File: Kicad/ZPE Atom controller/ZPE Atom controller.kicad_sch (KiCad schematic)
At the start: 48 parts, among them IC1 TC4424AVPA, J1 50 ohm 21 turns, P1 CONN_01X18, P2 CONN_01X18, Q1 2N2222, Q2 IRF3205, SW1 ON/OFF, SW2 SW_SPST, SW3 SW_SPST, SW4 SW_SPST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

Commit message: Added caps to inputs of the pots.
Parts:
- added C11, C12, C13, C14, C15: 100nF, Capacitor_THT:C_Disc_D5.0mm_W2.5mm_P5.00mm, symbol Device:C
- C10, C9: value 10nF -> 100nF
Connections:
- net GND: now also C11.2, C12.2, C13.2, C14.2, C15.2
- net IO32: now also C12.1
- net IO34: now also C14.1
- net IO35: now also C15.1
- net IO36: now also C13.1
- net IO39: now also C11.1
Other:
- moved on the sheet: DutyCycle1, Freq_fine1, Freq_rough1, Freq_super_fine1, Resolution1

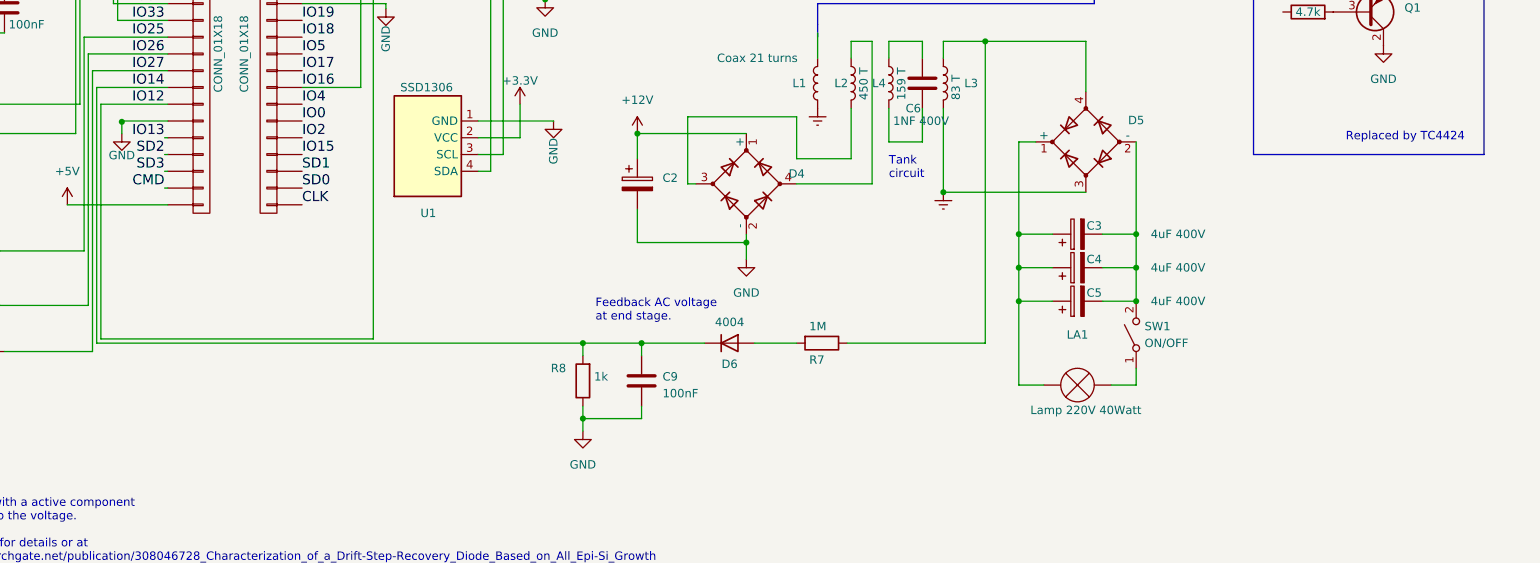
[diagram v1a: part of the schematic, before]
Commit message: Added DC to AC inverter
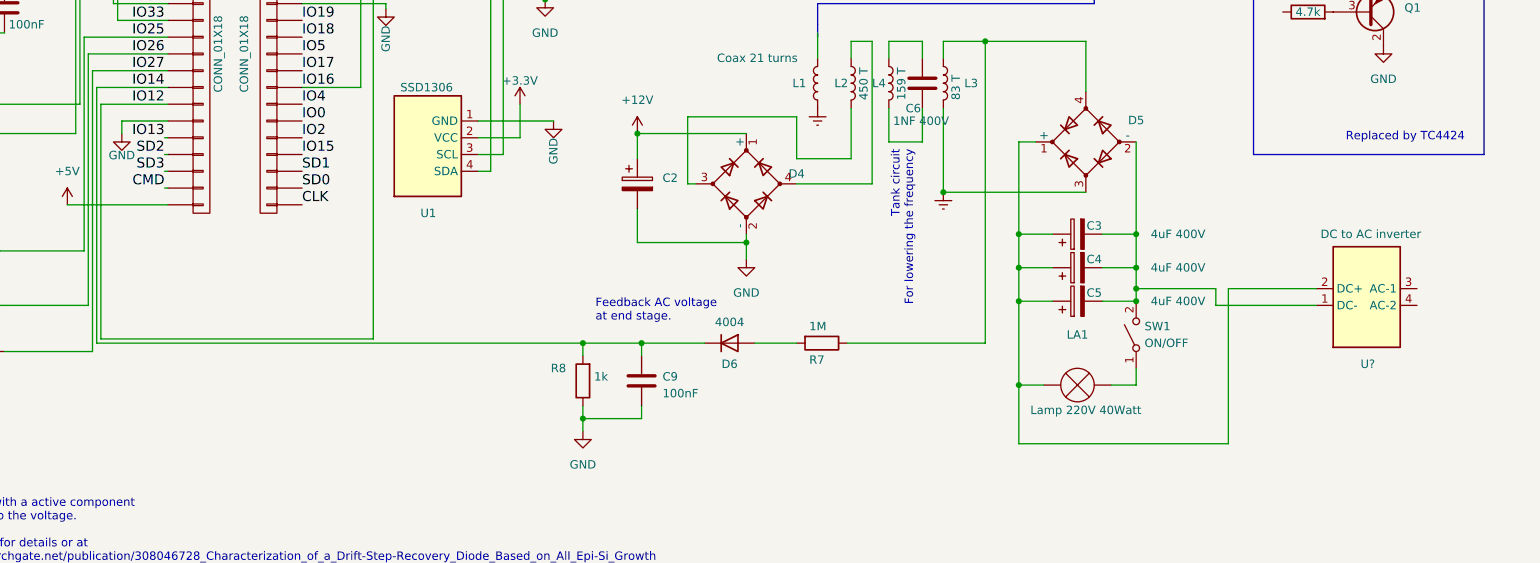
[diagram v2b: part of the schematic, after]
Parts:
- added U?: DC to AC inverter, DC to AC inverter, symbol Memory_EEPROM:24AA02-OT
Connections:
- net at C3.1, C4.1, C5.1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: now also U?.2 (DC+)
- net at C3.2, C4.2, C5.2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: now also U?.1 (DC-)
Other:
- note added: "Tank circuit For lowering the frequency"
- note removed: "Tank circuit"
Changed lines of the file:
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@@
   (junction (at 137.16 147.955) (diameter 0) (color 0 0 0 0)
   )
+  (junction (at 203.2 154.305) (diameter 0) (color 0 0 0 0)
+  )
   (junction (at 51.435 91.44) (diameter 0) (color 0 0 0 0)
   )
@@
   (junction (at 22.606 127) (diameter 0) (color 0 0 0 0)
   )
+  (junction (at 220.98 139.7) (diameter 0) (color 0 0 0 0)
+  )
   (junction (at 66.675 66.04) (diameter 0) (color 0 0 0 0)
   )
@@
   (junction (at 170.18 27.305) (diameter 0) (color 0 0 0 0)
   )
-  (junction (at 67.31 114.427) (diameter 0) (color 0 0 0 0)
-  )
   (junction (at 33.02 127) (diameter 0) (color 0 0 0 0)
   )
@@
     (stroke (width 0) (type default))
   )
+  (wire (pts (xy 248.285 139.7) (xy 234.95 139.7))
+    (stroke (width 0) (type default))
+  )
   (wire (pts (xy 123.19 86.36) (xy 123.19 121.92))
     (stroke (width 0) (type default))
@@
     (stroke (width 0) (type default))
   )
+  (wire (pts (xy 233.045 139.7) (xy 233.045 142.24))
+    (stroke (width 0) (type default))
+  )
   (wire (pts (xy 215.9 131.445) (xy 220.98 131.445))
     (stroke (width 0) (type default))
@@
     (stroke (width 0) (type default))
   )
+  (wire (pts (xy 220.98 139.7) (xy 220.98 136.525))
+    (stroke (width 0) (type default))
+  )
   (wire (pts (xy 46.355 100.965) (xy 36.195 100.965))
     (stroke (width 0) (type default))
@@
     (stroke (width 0) (type default))
   )
-  (wire (pts (xy 67.31 114.427) (xy 67.31 114.3))
-    (stroke (width 0) (type default))
-  )
   (wire (pts (xy 208.28 141.605) (xy 203.2 141.605))
     (stroke (width 0) (type default))
@@
     (stroke (width 0) (type default))
   )
+  (wire (pts (xy 233.045 139.7) (xy 220.98 139.7))
+    (stroke (width 0) (type default))
+  )
   (wire (pts (xy 49.53 93.345) (xy 51.435 93.345))
     (stroke (width 0) (type default))
@@
     (stroke (width 0) (type default))
   )
+  (wire (pts (xy 203.2 163.195) (xy 203.2 154.305))
+    (stroke (width 0) (type default))
+  )
   (wire (pts (xy 170.18 46.355) (xy 170.18 48.895))
     (stroke (width 0) (type default))
@@
     (stroke (width 0) (type default))
   )
-  (wire (pts (xy 67.31 114.427) (xy 67.31 116.205))
+  (wire (pts (xy 67.31 114.3) (xy 67.31 116.205))
     (stroke (width 0) (type default))
   )
@@
     (stroke (width 0) (type default))
   )
+  (wire (pts (xy 234.95 163.195) (xy 203.2 163.195))
+    (stroke (width 0) (type default))
+  )
   (wire (pts (xy 145.415 116.205) (xy 161.925 116.205))
     (stroke (width 0) (type default))
@@
     (stroke (width 0) (type default))
   )
-  (wire (pts (xy 220.98 141.605) (xy 220.98 136.525))
+  (wire (pts (xy 220.98 141.605) (xy 220.98 139.7))
     (stroke (width 0) (type default))
   )
@@
     (stroke (width 0) (type default))
   )
+  (wire (pts (xy 234.95 139.7) (xy 234.95 163.195))
+    (stroke (width 0) (type default))
+  )
   (wire (pts (xy 33.02 110.49) (xy 33.02 112.395))
+    (stroke (width 0) (type default))
+  )
+  (wire (pts (xy 233.045 142.24) (xy 248.285 142.24))
     (stroke (width 0) (type default))
   )
@@
     (effects (font (size 1.27 1.27)) (justify left bottom))
   )
-  (text "Tank \ncircuit" (at 183.515 123.19 0)
-    (effects (font (size 1.27 1.27)) (justify left bottom))
+  (text "Tank circuit\nFor lowering the frequency" (at 187.325 118.745 90)
+    (effects (font (size 1.27 1.27)) (justify right bottom))
   )
   (text "IRF3205 max freq 100K\nIRF840 max freq 500K" (at 172.085 77.47 0)
@@
     )
     (pin "1")
+  )
+  (symbol (lib_name "24AA02-OT_1") (lib_id "Memory_EEPROM:24AA02-OT") (at 255.905 140.97 0) (unit 1)
+    (in_bom yes) (on_board yes)
+    (property "Reference" "U?" (id 0) (at 257.175 151.13 0)
+      (effects (font (size 1.27 1.27)) (justify right))
+    )
+    (property "Value" "DC to AC inverter" (id 1) (at 264.16 131.445 0)
+      (effects (font (size 1.27 1.27)) (justify right))
+    )
+    (property "Footprint" "DC to AC inverter" (id 2) (at 255.905 140.97 0)
+      (effects (font (size 1.27 1.27)) hide)
+    )
+    (property "Datasheet" "" (id 3) (at 255.905 149.86 0)
+      (effects (font (size 1.27 1.27)) hide)
+    )
+    (pin "1")
+    (pin "2")
+    (pin "3")
+    (pin "4")
+    (pin "5")
   )
   (symbol (lib_id "Device:L") (at 191.77 108.585 180) (unit 1)
@@
       (reference "U1") (unit 1) (value "SSD1306") (footprint "Package_TO_SOT_SMD:SOT-23-5")
     )
-  )
+    (path "/111be01c-3f3d-4a63-a730-20593490b837"
+      (reference "U?") (unit 1) (value "DC to AC inverter") (footprint "DC to AC inverter")
+    )
+  )

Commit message: Updated and cleaned out the code
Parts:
- added SW5: RotaryEncoder_Switch, symbol Device:RotaryEncoder_Switch
- C7: value 1NF 1.5K -> 1NF 1.5kV
- L2: value 450 T -> 83T
- gave numbers to parts that had none: 1
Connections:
- net +12V: no longer C8.1
- net GND: now also SW5.C, SW5.S2
- net IO15: now also SW5.B
- net IO17: now also SW5.S1
- net IO2: now also SW5.A
- net at L5.1, R6.3: now also C8.1
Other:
- moved on the sheet: C8, R6

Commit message: Updated files
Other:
- note added: "IRF3205 max freq 100KHZ IRF840 max freq 500KHZ"
- note removed: "IRF3205 max freq 100K IRF840 max freq 500K"

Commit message: Updated schemtic
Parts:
- U: renamed from C2; value C_Polarized -> (none)
- U: renamed from SW2; value SW_SPST -> (none)
- U: renamed from LA1; value Lamp 220V 40Watt -> (none)
- U: renamed from C5; value 4uF 400V -> (none)
- U: renamed from C12; value 100nF -> (none); footprint Capacitor_THT:C_Disc_D5.0mm_W2.5mm_P5.00mm -> (none)
- U: renamed from U2; value DC to AC inverter -> (none); footprint DC to AC inverter -> (none)
- U: renamed from L3; value 83 T -> (none)
- U: renamed from C11; value 100nF -> (none); footprint Capacitor_THT:C_Disc_D5.0mm_W2.5mm_P5.00mm -> (none)
- U: renamed from Freq_rough1; value 10K -> (none); footprint Potentiometer_THT:Potentiometer_Piher_PC-16_Single_Vertical -> (none)
- U: renamed from Freq_fine1; value 10K -> (none); footprint Potentiometer_THT:Potentiometer_Piher_PC-16_Single_Vertical -> (none)
- U: renamed from R5; value 1K -> (none); footprint Resistor_THT:R_Axial_DIN0207_L6.3mm_D2.5mm_P10.16mm_Horizontal -> (none)
- U: renamed from R8; value 1k -> (none); footprint Resistor_THT:R_Axial_DIN0207_L6.3mm_D2.5mm_P10.16mm_Horizontal -> (none)
- U: renamed from C4; value 4uF 400V -> (none)
- U: renamed from D2; value D524 -> (none); footprint Diode_SMD:D_MELF -> (none)
- U: renamed from IC1; value TC4424AVPA -> (none); footprint Package_DIP:DIP-8_W10.16mm -> (none)
- U: renamed from L1; value Coax 21 turns -> (none)
- U: renamed from P2; value CONN_01X18 -> (none); footprint Connector_PinHeader_2.54mm:PinHeader_1x19_P2.54mm_Vertical -> (none)
- U: renamed from P1; value CONN_01X18 -> (none); footprint Connector_PinHeader_2.54mm:PinHeader_1x19_P2.54mm_Vertical -> (none)
- U: renamed from SW1; value ON/OFF -> (none)
- U: renamed from SW3; value SW_SPST -> (none)
- U: renamed from D5; value D_Bridge_+-AA -> (none)
- U: renamed from L5; value 330uH -> (none)
- U: renamed from C6; value 1NF 400V -> (none); footprint Capacitor_THT:C_Disc_D5.0mm_W2.5mm_P5.00mm -> (none)
- U: renamed from DutyCycle1; value 10k -> (none); footprint Potentiometer_THT:Potentiometer_Piher_PC-16_Single_Vertical -> (none)
- U: renamed from C7; value 1NF 1.5kV -> (none)
- U: renamed from J1; value 50 ohm 21 turns -> (none)
- U: renamed from C10; value 100nF -> (none); footprint Capacitor_THT:C_Disc_D5.0mm_W2.5mm_P5.00mm -> (none)
- U: renamed from C3; value 4uF 400V -> (none)
- U: renamed from L2; value 83T -> (none)
- U: renamed from D3; value D524 -> (none); footprint Diode_SMD:D_MELF -> (none)
- U: renamed from R3; value 4.7k -> (none); footprint Resistors_THT:R_Axial_DIN0204_L3.6mm_D1.6mm_P7.62mm_Horizontal -> (none)
- U: renamed from T1; value Transformer_SP_1S -> (none); footprint Transformer_THT:Transformer_NF_ETAL_P1165 -> (none)
- U: renamed from C14; value 100nF -> (none); footprint Capacitor_THT:C_Disc_D5.0mm_W2.5mm_P5.00mm -> (none)
- U: renamed from C13; value 100nF -> (none); footprint Capacitor_THT:C_Disc_D5.0mm_W2.5mm_P5.00mm -> (none)
- U: renamed from C9; value 100nF -> (none); footprint Capacitor_THT:C_Disc_D5.0mm_W2.5mm_P5.00mm -> (none)
- U: renamed from R2; value 1k -> (none); footprint Resistor_THT:R_Axial_DIN0207_L6.3mm_D2.5mm_P10.16mm_Horizontal -> (none)
- U: renamed from Resolution1; value 10K -> (none); footprint Potentiometer_THT:Potentiometer_Piher_PC-16_Single_Vertical -> (none)
- U: renamed from R7; value 1M -> (none); footprint Resistor_THT:R_Axial_DIN0207_L6.3mm_D2.5mm_P10.16mm_Horizontal -> (none)
- U: renamed from R1; value 4.7k -> (none); footprint Resistor_THT:R_Axial_DIN0207_L6.3mm_D2.5mm_P10.16mm_Horizontal -> (none)
- U: renamed from Q1; value 2N2222 -> (none)
- U: renamed from D6; value 4004 -> (none); footprint Diode_SMD:D_MELF -> (none)
- U: renamed from C15; value 100nF -> (none); footprint Capacitor_THT:C_Disc_D5.0mm_W2.5mm_P5.00mm -> (none)
- U: renamed from D4; value D_Bridge_+-AA -> (none)
- U: renamed from U1; value SSD1306 -> (none); footprint Package_TO_SOT_SMD:SOT-23-5 -> (none)
- U: renamed from D1; value D524 -> (none); footprint Diode_SMD:D_MELF -> (none)
- U: renamed from C1; value 1NF 1.5K -> (none)
- U: renamed from Freq_super_fine1; value 10k -> (none); footprint Potentiometer_THT:Potentiometer_Piher_PC-16_Single_Vertical -> (none)
- U: renamed from R9; value 1M -> (none); footprint Resistor_THT:R_Axial_DIN0207_L6.3mm_D2.5mm_P10.16mm_Horizontal -> (none)
- U: renamed from SW5; value RotaryEncoder_Switch -> (none)
- U: renamed from L4; value 159 T -> (none)
- U: renamed from C8; value 1000uF -> (none)
- U: renamed from D7; value 4004 -> (none); footprint Diode_SMD:D_MELF -> (none)
- U: renamed from Q2; value IRF3205 -> (none); footprint Housings_SIP:SIP3_11.6x8.5mm -> (none)
- U: renamed from SW4; value SW_SPST -> (none)
- U: renamed from R6; value 100 -> (none); footprint Potentiometer_THT:Potentiometer_Piher_T-16L_Single_Vertical_Hole -> (none)

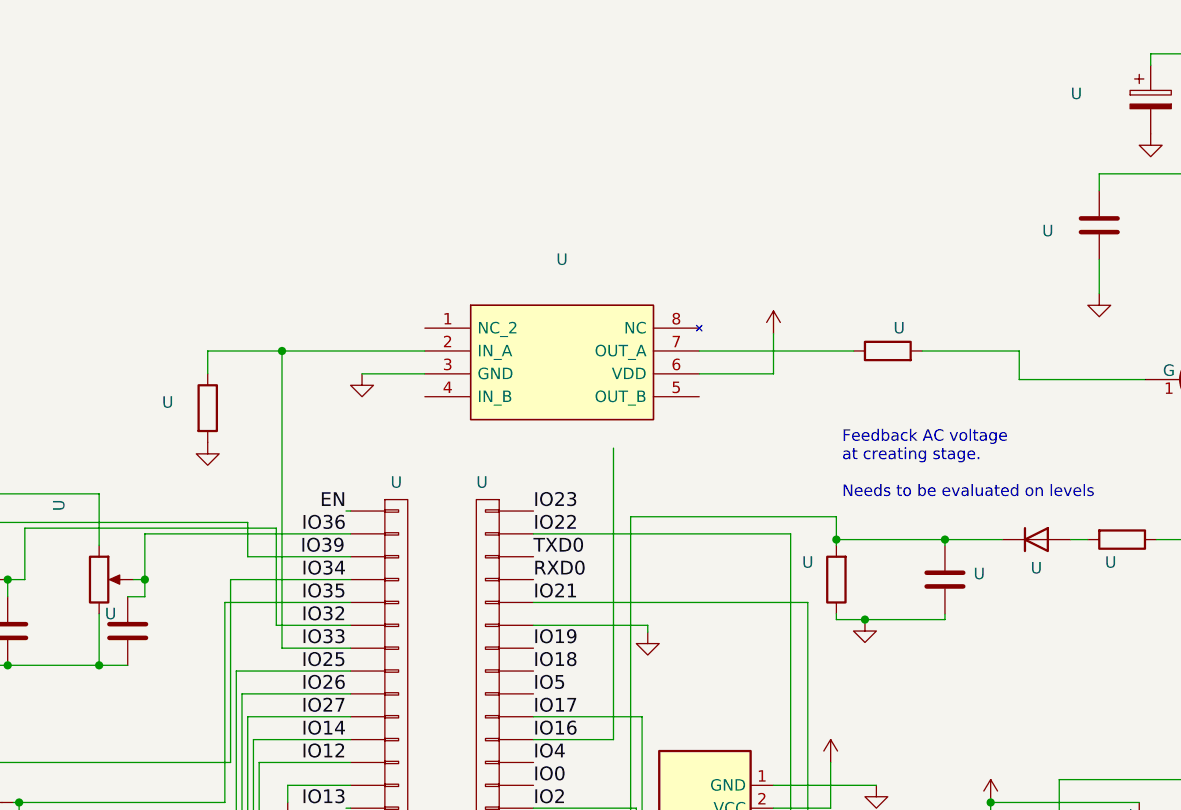
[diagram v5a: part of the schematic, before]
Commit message: Added hex inverter 4006 to the schematic
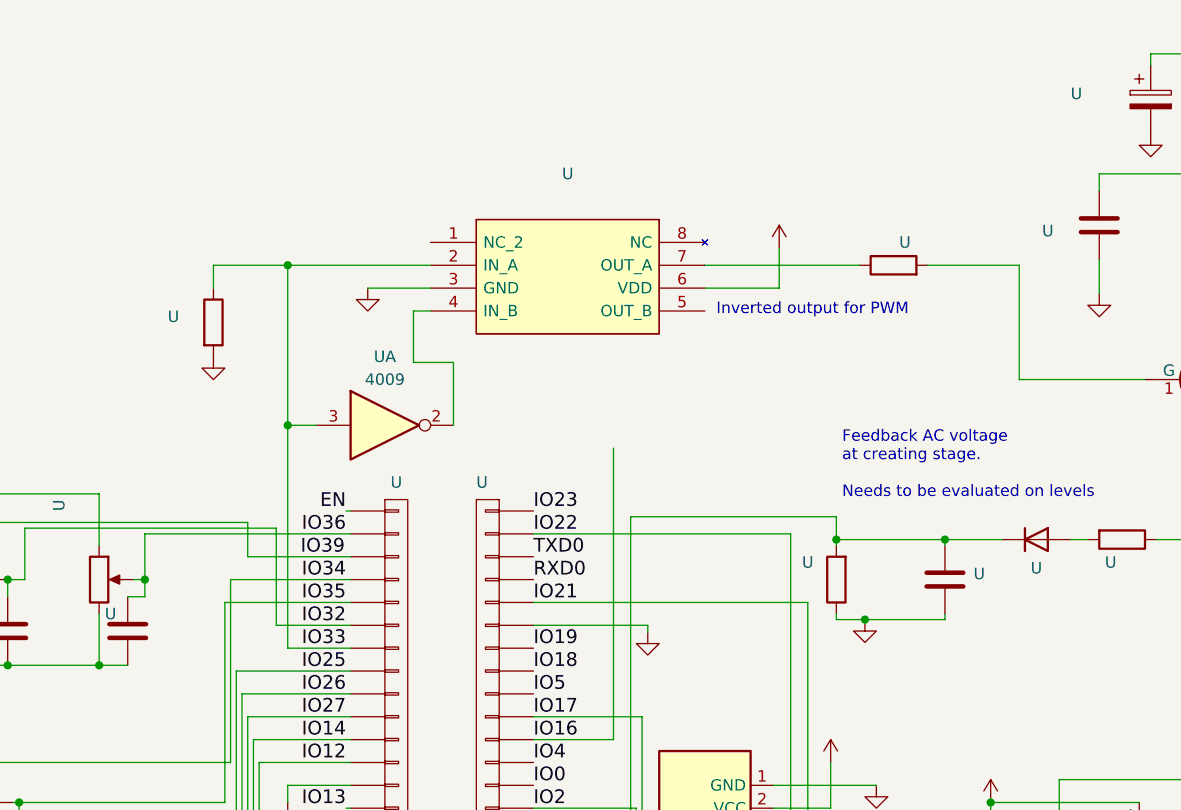
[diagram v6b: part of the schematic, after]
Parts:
- added U: 4009, symbol 4xxx:4009
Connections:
- net IO33: now also U.3
- net at U.4 (IN_B): now also U.2
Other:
- note added: "Inverted output for PWM"
- moved on the sheet: U
